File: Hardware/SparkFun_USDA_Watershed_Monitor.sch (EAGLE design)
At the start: 108 parts, among them J10 QWIIC_RIGHT_ANGLE, J3 QWIIC_RIGHT_ANGLE, J4 U.FL, J5 RJ45, J7 RJ45, J9 RJ45, Q1 20V/4.2A/52mΩ/1.4W, Q2 20V/0.2A/8MHz/1.2Ω/1Vth, Q3 20V/0.2A/8MHz/1.2Ω/1Vth, Q4 20V/0.2A/8MHz/1.2Ω/1Vth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

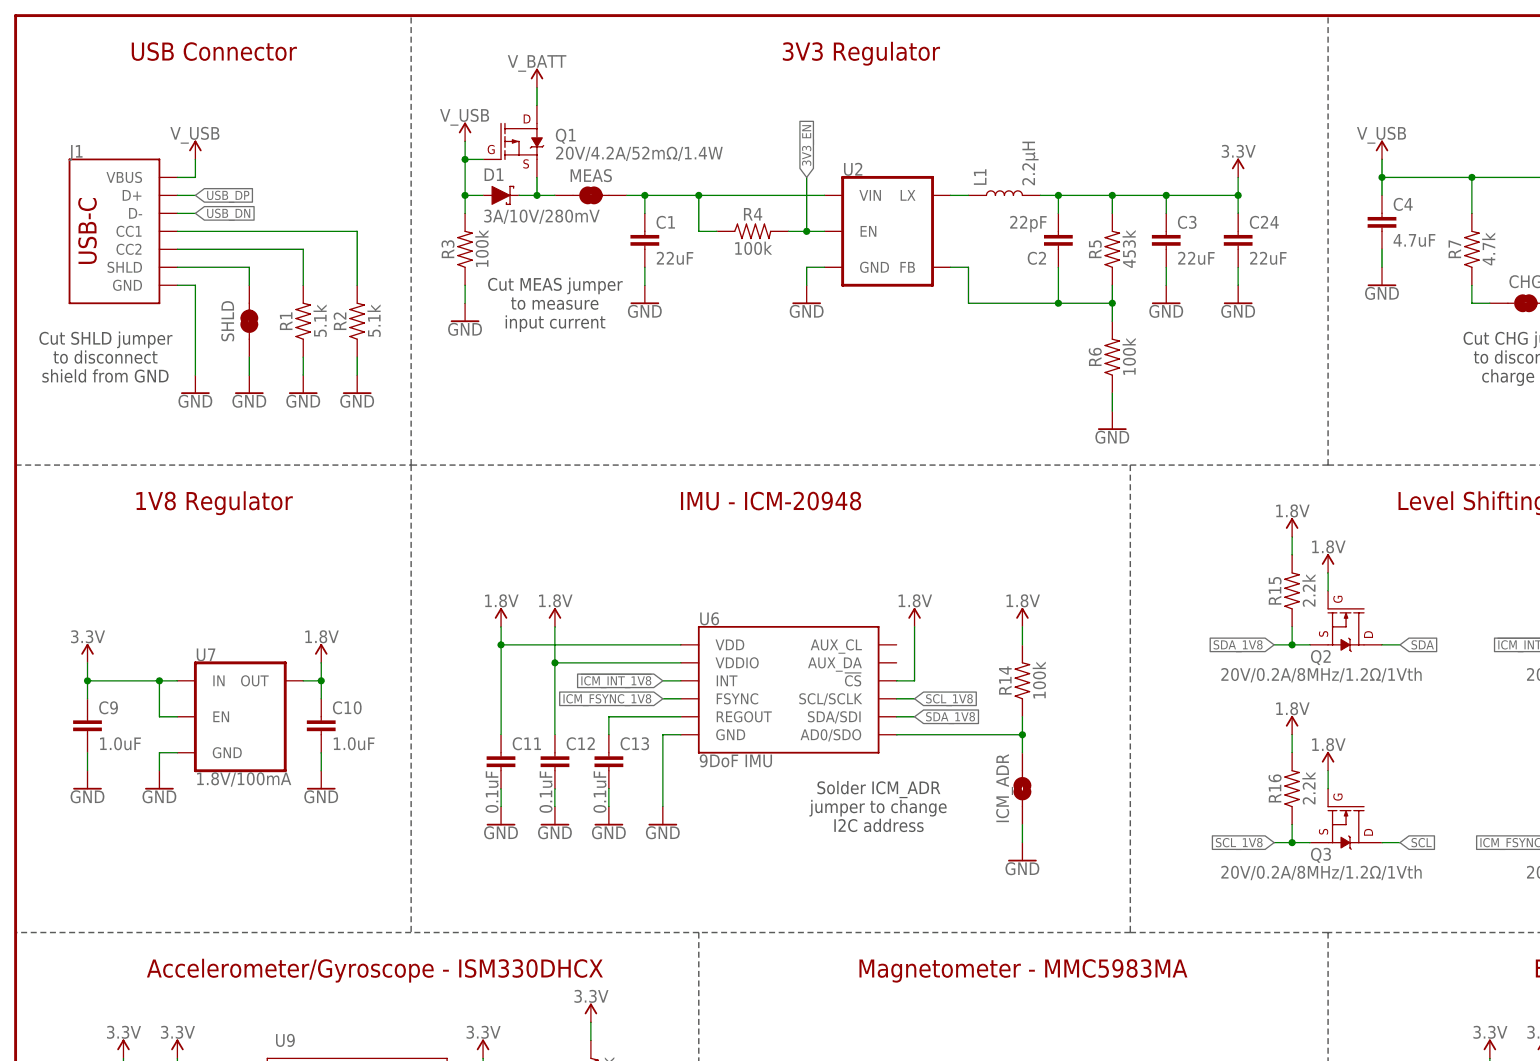
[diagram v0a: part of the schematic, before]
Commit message: Add 5V header
Add 5V header for power injection
Rename V_USB  net to 5V
Add diode to USB input to protect against 5V contention
Header  took place of I2C pullups, so those got moved to other side of Qwiic connector
Add units to measures
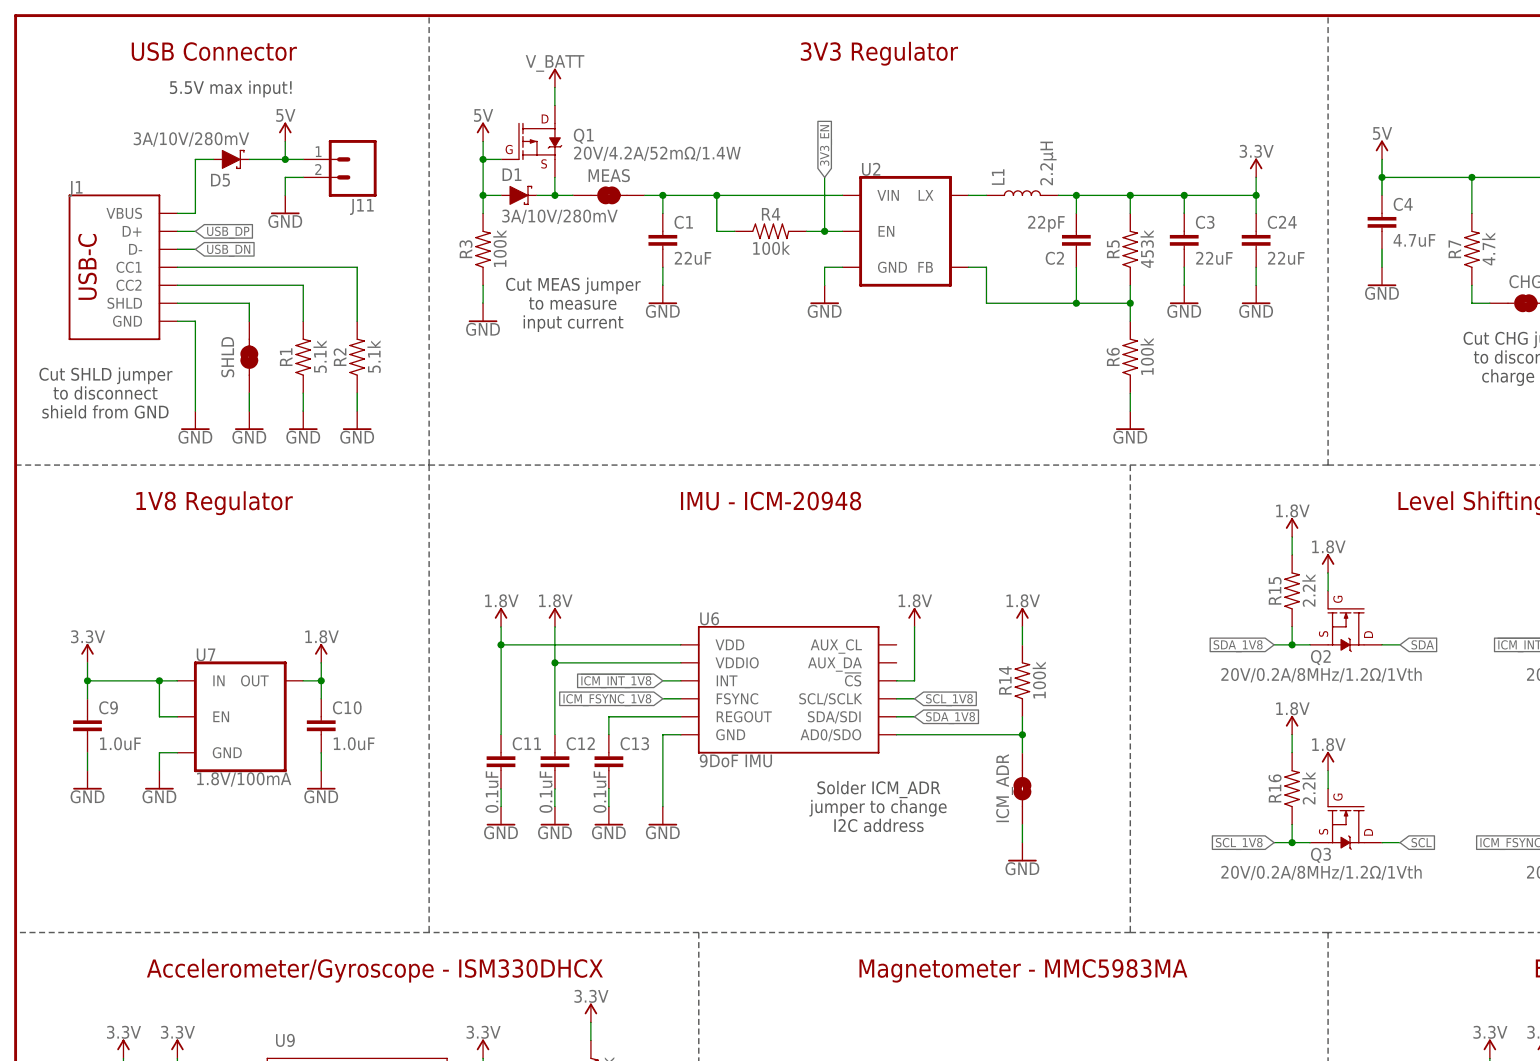
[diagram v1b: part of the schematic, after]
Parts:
- added D5: 3A/10V/280mV, SparkFun-DiscreteSemi:DIODE-SCHOTTKY-BAT60A
- added J11: (no value), SparkFun-Connectors:CONN_021X02_NO_SILK
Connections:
- new net 5V: C4.1, D1.A, D5.C, J11.1, Q1.G, R3.2, R7.2, U3.VIN
- net GND: now also J11.2
- net V_USB: now also D5.A; no longer C4.1, D1.A, Q1.G, R3.2, R7.2, U3.VIN
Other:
- note added: "5.5V max input!"
- moved on the sheet: C1, C2, C24, C3, D1, J1, L1, MEAS, Q1, R1, R2, R3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

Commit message: Schematic review updates
Add note about ICM-20948 going EOL
Add I2C addresses of all sensors
Add max input voltage to regulators
Add value to 3V3 regulator
Add boot table to auto reset
Change power LED resistor to 1k
Move load cell connector with other connectors
Remove bar from interrupt net names
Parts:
- R10: value 2.2k -> 1k; device SparkFun-Resistors:2.2KOHM-0603-1/10W-1% -> SparkFun-Resistors:1KOHM-0603-1/10W-1%
- U2: value (none) -> AP3429A
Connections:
- net !ICM_INT! renamed ICM_INT
- net !ISM_INT1! renamed ISM_INT1
- net !ISM_INT2! renamed ISM_INT2
- net !MMC_INT! renamed MMC_INT
- net !NAU_INT! renamed NAU_INT
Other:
- note added: "0"
- note added: "1"
- note added: "Boot Mode Configuration"
- note added: "Bootloader"
- note added: "DTR LOW and RTS HIGH to LOW - resets to run mode RTS HIGH and DTR LOW to HIGH - resets to bootloader"
- note added: "Default"
- note added: "I2C address: 0x2A"
- note added: "I2C default address: 0x69 Close ICM_ADR: 0x68"
- note added: "I2C default address: 0x6B Close ISM_ADR: 0x6A"
- note added: "I2C default address: 0x77 Close BME_ADR: 0x76"
- note added: "IO0"
- note added: "IO12"
- note added: "IO15"
- note added: "IO2"
- note added: "IO5"
- note added: "If the ICM-20948 goes EOL, it will be substituted for ISM330DHCX and MMC5983MA. Those parts will remain unpopulated until then."
- note added: "Max input: 5.5V"
- note added: "Max input: 7V"
- note added: "Pin"
- note added: "Run"
- note added: "x"
- note removed: "5.5V max input!"
- note removed: "Solder BME_ADR jumper to change I2C address"
- note removed: "Solder ICM_ADR jumper to change I2C address"
- note removed: "Solder ISM_ADR jumper to change I2C address"
- moved on the sheet: C11, C12, C13, C15, C16, C19, C20, C21, C22, C23, ICM_ADR, ISM_ADR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

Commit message: Design review updates
Replace "VUSB" buzzard label with "5V"
Add test point for 1.8V net
Nudge C22 to the left
Add selective solder paths
Move u.FL connector away from board edge
Nudge GPIO lines under load cell connector to the left
Rename GPIO nets that aren't broken out to connectors with more helpful names
Fix CH340 capacitors (100nF on VCC only, add 10nF to V3 and disconnect from 3.3V net)
Move USB connector to not overhang edge (better for panelization)
Move CC resistors and VUSB diode next to battery PTH pads
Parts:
- added C6: 10nF, SparkFun-Capacitors:10NF-0603-50V-10%
- added TP1: TEST-POINT3X4, SparkFun-Connectors:TEST-POINT3X4
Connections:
- net !ICM_INT_1V8! renamed ICM_INT_1V8
- net ESP_IO0 renamed ESP_IO0_BOOT
- net ESP_IO2 renamed STAT
- net ESP_IO32 renamed V_BATT_2
- net ESP_IO4 renamed ESP_INT_COM
- new net N$12: C6.1, U8.V3
- net 1.8V: now also TP1.1
- net 3.3V: no longer U8.V3
- net GND: now also C6.2
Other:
- moved on the sheet: C14, J4, U11, U8

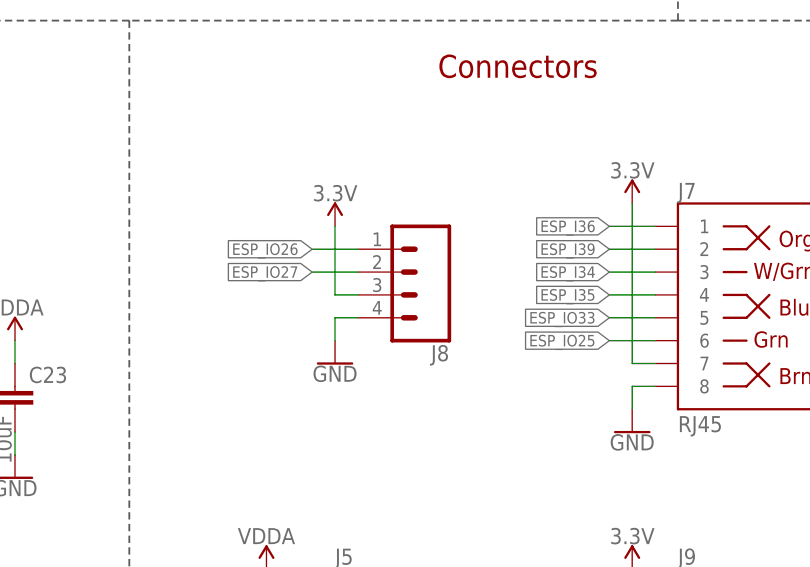
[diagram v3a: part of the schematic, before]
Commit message: Move load cell connector to bottom edge
Will help a lot with panelization
Moved left GPIO RJ45 connector to bottom middle, and redid connections for easier routing
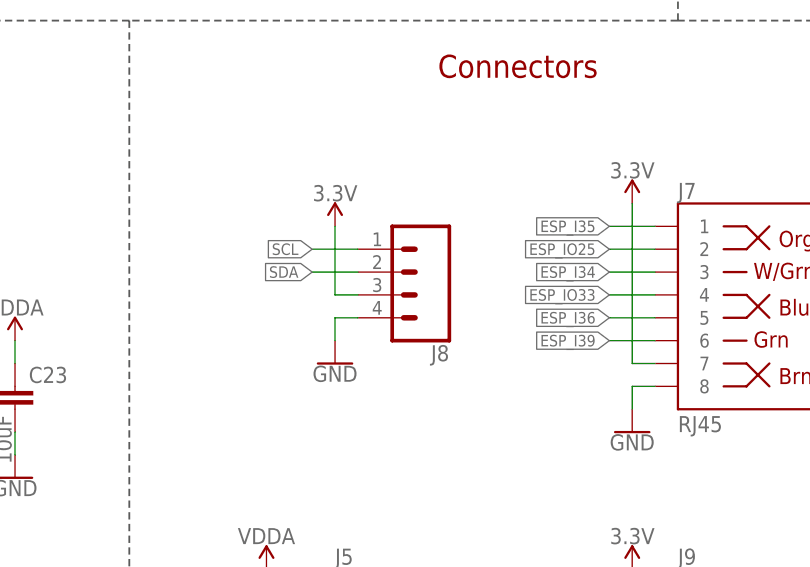
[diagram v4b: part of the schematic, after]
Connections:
- net ESP_I35: now also J7.1; no longer J7.4
- net ESP_I36: now also J7.5; no longer J7.1
- net ESP_I39: now also J7.6; no longer J7.2
- net ESP_IO25: now also J7.2; no longer J7.6
- net ESP_IO26: no longer J8.1
- net ESP_IO27: no longer J8.2
- net ESP_IO33: now also J7.4; no longer J7.5
- net SCL: now also J8.1
- net SDA: now also J8.2
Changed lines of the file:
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@@
 <part name="SUPPLY44" library="SparkFun-PowerSymbols" deviceset="3.3V" device=""/>
 <part name="GND19" library="SparkFun-PowerSymbols" deviceset="GND" device=""/>
-<part name="SUPPLY47" library="SparkFun-PowerSymbols" deviceset="3.3V" device=""/>
-<part name="GND20" library="SparkFun-PowerSymbols" deviceset="GND" device=""/>
 <part name="R9" library="SparkFun-Resistors" deviceset="100KOHM" device="-0603-1/10W-1%" value="100k"/>
 <part name="R25" library="SparkFun-Resistors" deviceset="100KOHM" device="-0603-1/10W-1%" value="100k"/>
@@
 <part name="C6" library="SparkFun-Capacitors" deviceset="10NF" device="-0603-50V-10%" value="10nF"/>
 <part name="GND58" library="SparkFun-PowerSymbols" deviceset="GND" device=""/>
+<part name="GND59" library="SparkFun-PowerSymbols" deviceset="GND" device=""/>
+<part name="SUPPLY6" library="SparkFun-PowerSymbols" deviceset="3.3V" device=""/>
 </parts>
 <sheets>
@@
 <attribute name="VALUE" x="302.26" y="7.366" size="1.778" layer="96" font="vector" align="top-center"/>
 </instance>
-<instance part="SUPPLY47" gate="G$1" x="269.24" y="71.12" smashed="yes">
-<attribute name="VALUE" x="269.24" y="73.914" size="1.778" layer="96" font="vector" align="bottom-center"/>
-</instance>
-<instance part="GND20" gate="1" x="269.24" y="55.88" smashed="yes">
-<attribute name="VALUE" x="269.24" y="55.626" size="1.778" layer="96" font="vector" align="top-center"/>
-</instance>
 <instance part="R9" gate="G$1" x="281.94" y="172.72" smashed="yes" rot="R90">
 <attribute name="NAME" x="280.416" y="172.72" size="1.778" layer="95" font="vector" rot="R90" align="bottom-center"/>
@@
 <instance part="GND58" gate="1" x="320.04" y="233.68" smashed="yes">
 <attribute name="VALUE" x="320.04" y="233.426" size="1.778" layer="96" font="vector" align="top-center"/>
+</instance>
+<instance part="GND59" gate="1" x="269.24" y="55.88" smashed="yes" rot="MR0">
+<attribute name="VALUE" x="269.24" y="55.626" size="1.778" layer="96" font="vector" rot="MR0" align="top-center"/>
+</instance>
+<instance part="SUPPLY6" gate="G$1" x="269.24" y="71.12" smashed="yes" rot="MR0">
+<attribute name="VALUE" x="269.24" y="73.914" size="1.778" layer="96" font="vector" rot="MR0" align="bottom-center"/>
 </instance>
 </instances>
@@
 </segment>
 <segment>
-<pinref part="GND20" gate="1" pin="GND"/>
-<wire x1="269.24" y1="58.42" x2="269.24" y2="60.96" width="0.1524" layer="91"/>
-<wire x1="269.24" y1="60.96" x2="271.78" y2="60.96" width="0.1524" layer="91"/>
-<pinref part="J8" gate="J1" pin="4"/>
-</segment>
-<segment>
 <pinref part="J7" gate="JP1" pin="8"/>
 <pinref part="GND14" gate="1" pin="GND"/>
@@
 <wire x1="320.04" y1="236.22" x2="320.04" y2="238.76" width="0.1524" layer="91"/>
 <pinref part="C6" gate="G$1" pin="2"/>
+</segment>
+<segment>
+<pinref part="GND59" gate="1" pin="GND"/>
+<wire x1="271.78" y1="60.96" x2="269.24" y2="60.96" width="0.1524" layer="91"/>
+<wire x1="269.24" y1="60.96" x2="269.24" y2="58.42" width="0.1524" layer="91"/>
+<pinref part="J8" gate="J1" pin="4"/>
 </segment>
 </net>
@@
 </segment>
 <segment>
-<pinref part="SUPPLY47" gate="G$1" pin="3.3V"/>
-<wire x1="271.78" y1="63.5" x2="269.24" y2="63.5" width="0.1524" layer="91"/>
-<wire x1="269.24" y1="63.5" x2="269.24" y2="71.12" width="0.1524" layer="91"/>
-<pinref part="J8" gate="J1" pin="3"/>
-</segment>
-<segment>
 <pinref part="J7" gate="JP1" pin="7"/>
 <pinref part="SUPPLY10" gate="G$1" pin="3.3V"/>
@@
 <wire x1="302.26" y1="15.24" x2="302.26" y2="33.02" width="0.1524" layer="91"/>
 </segment>
+<segment>
+<pinref part="SUPPLY6" gate="G$1" pin="3.3V"/>
+<wire x1="271.78" y1="63.5" x2="269.24" y2="63.5" width="0.1524" layer="91"/>
+<wire x1="269.24" y1="63.5" x2="269.24" y2="71.12" width="0.1524" layer="91"/>
+<pinref part="J8" gate="J1" pin="3"/>
+</segment>
 </net>
 <net name="N$8" class="0">
@@
 <label x="378.46" y="160.02" size="1.27" layer="95" font="vector" rot="R180" xref="yes"/>
 </segment>
+<segment>
+<wire x1="271.78" y1="68.58" x2="266.7" y2="68.58" width="0.1524" layer="91"/>
+<label x="266.7" y="68.58" size="1.27" layer="95" font="vector" rot="MR0" xref="yes"/>
+<pinref part="J8" gate="J1" pin="1"/>
+</segment>
 </net>
 <net name="SDA" class="0">
@@
 <wire x1="416.56" y1="160.02" x2="419.1" y2="160.02" width="0.1524" layer="91"/>
 <label x="419.1" y="160.02" size="1.27" layer="95" font="vector" xref="yes"/>
+</segment>
+<segment>
+<label x="266.7" y="66.04" size="1.27" layer="95" font="vector" rot="MR0" xref="yes"/>
+<wire x1="271.78" y1="66.04" x2="266.7" y2="66.04" width="0.1524" layer="91"/>
+<pinref part="J8" gate="J1" pin="2"/>
 </segment>
 </net>
@@
 </segment>
 <segment>
-<wire x1="304.8" y1="58.42" x2="299.72" y2="58.42" width="0.1524" layer="91"/>
-<label x="299.72" y="58.42" size="1.27" layer="95" font="vector" rot="R180" xref="yes"/>
-<pinref part="J7" gate="JP1" pin="6"/>
+<wire x1="304.8" y1="68.58" x2="299.72" y2="68.58" width="0.1524" layer="91"/>
+<label x="299.72" y="68.58" size="1.27" layer="95" font="vector" rot="R180" xref="yes"/>
+<pinref part="J7" gate="JP1" pin="2"/>
 </segment>
 </net>
@@
 <label x="55.88" y="27.94" size="1.27" layer="95" font="vector" xref="yes"/>
 </segment>
-<segment>
-<wire x1="271.78" y1="68.58" x2="266.7" y2="68.58" width="0.1524" layer="91"/>
-<label x="266.7" y="68.58" size="1.27" layer="95" font="vector" rot="R180" xref="yes"/>
-<pinref part="J8" gate="J1" pin="1"/>
-</segment>
 </net>
 <net name="ESP_IO27" class="0">
@@
 <wire x1="53.34" y1="25.4" x2="55.88" y2="25.4" width="0.1524" layer="91"/>
 <label x="55.88" y="25.4" size="1.27" layer="95" font="vector" xref="yes"/>
-</segment>
-<segment>
-<wire x1="271.78" y1="66.04" x2="266.7" y2="66.04" width="0.1524" layer="91"/>
-<label x="266.7" y="66.04" size="1.27" layer="95" font="vector" rot="R180" xref="yes"/>
-<pinref part="J8" gate="J1" pin="2"/>
 </segment>
 </net>
@@
 </segment>
 <segment>
+<wire x1="304.8" y1="63.5" x2="299.72" y2="63.5" width="0.1524" layer="91"/>
+<label x="299.72" y="63.5" size="1.27" layer="95" font="vector" rot="R180" xref="yes"/>
+<pinref part="J7" gate="JP1" pin="4"/>
+</segment>
+</net>
+<net name="ESP_I34" class="0">
+<segment>
+<pinref part="U1" gate="U1" pin="IA34"/>
+<wire x1="53.34" y1="17.78" x2="55.88" y2="17.78" width="0.1524" layer="91"/>
+<label x="55.88" y="17.78" size="1.27" layer="95" font="vector" xref="yes"/>
+</segment>
+<segment>
+<wire x1="304.8" y1="66.04" x2="299.72" y2="66.04" width="0.1524" layer="91"/>
+<label x="299.72" y="66.04" size="1.27" layer="95" font="vector" rot="R180" xref="yes"/>
+<pinref part="J7" gate="JP1" pin="3"/>
+</segment>
+</net>
+<net name="ESP_I35" class="0">
+<segment>
+<pinref part="U1" gate="U1" pin="IA35"/>
+<wire x1="53.34" y1="15.24" x2="55.88" y2="15.24" width="0.1524" layer="91"/>
+<label x="55.88" y="15.24" size="1.27" layer="95" font="vector" xref="yes"/>
+</segment>
+<segment>
+<wire x1="304.8" y1="71.12" x2="299.72" y2="71.12" width="0.1524" layer="91"/>
+<label x="299.72" y="71.12" size="1.27" layer="95" font="vector" rot="R180" xref="yes"/>
+<pinref part="J7" gate="JP1" pin="1"/>
+</segment>
+</net>
+<net name="ESP_I36" class="0">
+<segment>
+<pinref part="U1" gate="U1" pin="SENSOR_VP/IA36"/>
+<wire x1="53.34" y1="12.7" x2="55.88" y2="12.7" width="0.1524" layer="91"/>
+<label x="55.88" y="12.7" size="1.27" layer="95" font="vector" xref="yes"/>
+</segment>
+<segment>
 <wire x1="304.8" y1="60.96" x2="299.72" y2="60.96" width="0.1524" layer="91"/>
 <label x="299.72" y="60.96" size="1.27" layer="95" font="vector" rot="R180" xref="yes"/>
@@
 </segment>
 </net>
-<net name="ESP_I34" class="0">
-<segment>
-<pinref part="U1" gate="U1" pin="IA34"/>
-<wire x1="53.34" y1="17.78" x2="55.88" y2="17.78" width="0.1524" layer="91"/>
-<label x="55.88" y="17.78" size="1.27" layer="95" font="vector" xref="yes"/>
-</segment>
-<segment>
-<wire x1="304.8" y1="66.04" x2="299.72" y2="66.04" width="0.1524" layer="91"/>
-<label x="299.72" y="66.04" size="1.27" layer="95" font="vector" rot="R180" xref="yes"/>
-<pinref part="J7" gate="JP1" pin="3"/>
-</segment>
-</net>
-<net name="ESP_I35" class="0">
-<segment>
-<pinref part="U1" gate="U1" pin="IA35"/>
-<wire x1="53.34" y1="15.24" x2="55.88" y2="15.24" width="0.1524" layer="91"/>
-<label x="55.88" y="15.24" size="1.27" layer="95" font="vector" xref="yes"/>
-</segment>
-<segment>
-<wire x1="304.8" y1="63.5" x2="299.72" y2="63.5" width="0.1524" layer="91"/>
-<label x="299.72" y="63.5" size="1.27" layer="95" font="vector" rot="R180" xref="yes"/>
-<pinref part="J7" gate="JP1" pin="4"/>
-</segment>
-</net>
-<net name="ESP_I36" class="0">
-<segment>
-<pinref part="U1" gate="U1" pin="SENSOR_VP/IA36"/>
-<wire x1="53.34" y1="12.7" x2="55.88" y2="12.7" width="0.1524" layer="91"/>
-<label x="55.88" y="12.7" size="1.27" layer="95" font="vector" xref="yes"/>
-</segment>
-<segment>
-<wire x1="304.8" y1="71.12" x2="299.72" y2="71.12" width="0.1524" layer="91"/>
-<label x="299.72" y="71.12" size="1.27" layer="95" font="vector" rot="R180" xref="yes"/>
-<pinref part="J7" gate="JP1" pin="1"/>
-</segment>
-</net>
 <net name="ESP_I39" class="0">
 <segment>
@@
 </segment>
 <segment>
-<wire x1="304.8" y1="68.58" x2="299.72" y2="68.58" width="0.1524" layer="91"/>
-<label x="299.72" y="68.58" size="1.27" layer="95" font="vector" rot="R180" xref="yes"/>
-<pinref part="J7" gate="JP1" pin="2"/>
-</segment>
-</net>
+<wire x1="304.8" y1="58.42" x2="299.72" y2="58.42" width="0.1524" layer="91"/>
+<label x="299.72" y="58.42" size="1.27" layer="95" font="vector" rot="R180" xref="yes"/>
+<pinref part="J7" gate="JP1" pin="6"/>
+</segment>
+</net>
